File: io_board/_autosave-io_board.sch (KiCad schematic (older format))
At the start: 0 parts

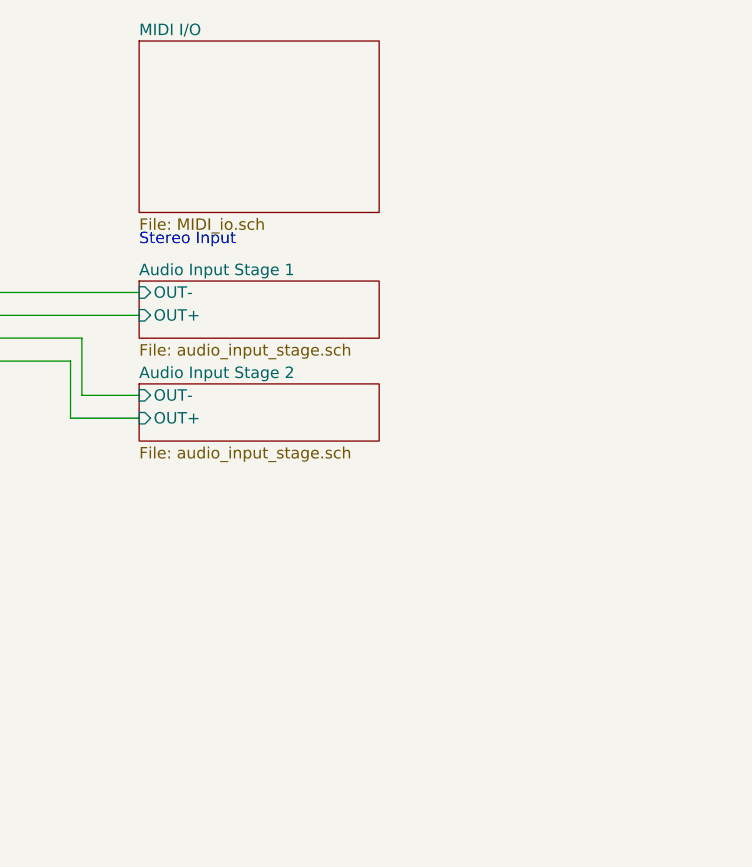
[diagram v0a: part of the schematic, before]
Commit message: Added MIDI connectors and SD card to io_board
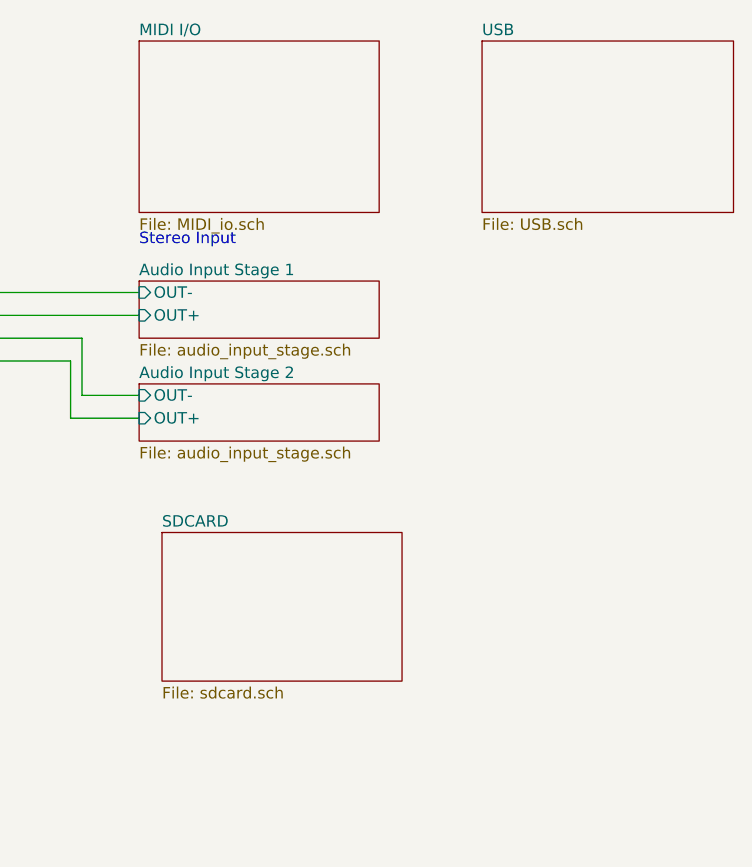
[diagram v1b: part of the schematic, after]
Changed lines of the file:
@@
 $Descr A4 11693 8268
 encoding utf-8
-Sheet 1 7
+Sheet 1 9
 Title ""
 Date ""
@@
 F1 "MIDI_io.sch" 50
 $EndSheet
+$Sheet
+S 3100 3150 1050 650
+U 5D472DBF
+F0 "SDCARD" 50
+F1 "sdcard.sch" 50
+$EndSheet
+$Sheet
+S 4500 1000 1100 750
+U 5D436844
+F0 "USB" 50
+F1 "USB.sch" 50
+$EndSheet
 $EndSCHEMATC
